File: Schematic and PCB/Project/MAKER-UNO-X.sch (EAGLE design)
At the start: 101 parts, among them CN1 USB-5PIN_(MICRO-B-RA), Q1 60V 600mA, Q10 50V 220mA, Q11 50V 220mA, Q12 50V 220mA, Q13 50V 220mA, Q14 50V 220mA, Q2 50V 220mA, Q3 50V 220mA, Q4 50V 220mA, Q5 50V 220mA, Q6 50V 220mA, Q7 50V 220mA, Q8 50V 220mA, Q9 50V 220mA, U2 CH340G_(SOIC-16N), U3 555_(SOIC-08N), U4 3.3V 500mA, Y1 16MHz

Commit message: Updated resistor value.
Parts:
- R11: value 10R -> 5R1; device Others:RESISTOR_10R_(2012) -> Others:RESISTOR_5R1_(2012)
- R4: value 1M -> 100K; device Others:RESISTOR_1M_(1608) -> Others:RESISTOR_100K_(1608)
- R5: value 22K -> 10K; device Others:RESISTOR_22K_(1608) -> Others:RESISTOR_10K_(1608)
- R9: value 1K -> 330R; device Others:RESISTOR_1K_(1608) -> Others:RESISTOR_330R_(1608)
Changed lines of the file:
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@@
 <grid distance="0.1" unitdist="inch" unit="inch" style="lines" multiple="1" display="no" altdistance="0.01" altunitdist="inch" altunit="inch"/>
 <layers>
-<layer number="1" name="Top" color="4" fill="1" visible="yes" active="no"/>
-<layer number="2" name="Route2" color="1" fill="3" visible="yes" active="no"/>
-<layer number="3" name="Route3" color="4" fill="3" visible="yes" active="no"/>
-<layer number="4" name="Route4" color="1" fill="4" visible="yes" active="no"/>
-<layer number="5" name="Route5" color="4" fill="4" visible="yes" active="no"/>
-<layer number="6" name="Route6" color="1" fill="8" visible="yes" active="no"/>
-<layer number="7" name="Route7" color="4" fill="8" visible="yes" active="no"/>
-<layer number="8" name="Route8" color="1" fill="2" visible="yes" active="no"/>
-<layer number="9" name="Route9" color="4" fill="2" visible="yes" active="no"/>
-<layer number="10" name="Route10" color="1" fill="7" visible="yes" active="no"/>
-<layer number="11" name="Route11" color="4" fill="7" visible="yes" active="no"/>
-<layer number="12" name="Route12" color="1" fill="5" visible="yes" active="no"/>
-<layer number="13" name="Route13" color="4" fill="5" visible="yes" active="no"/>
-<layer number="14" name="Route14" color="1" fill="6" visible="yes" active="no"/>
-<layer number="15" name="Route15" color="4" fill="6" visible="yes" active="no"/>
-<layer number="16" name="Bottom" color="1" fill="1" visible="yes" active="no"/>
-<layer number="17" name="Pads" color="2" fill="1" visible="yes" active="no"/>
-<layer number="18" name="Vias" color="2" fill="1" visible="yes" active="no"/>
-<layer number="19" name="Unrouted" color="6" fill="1" visible="yes" active="no"/>
-<layer number="20" name="Dimension" color="15" fill="1" visible="yes" active="no"/>
-<layer number="21" name="tPlace" color="7" fill="1" visible="yes" active="no"/>
-<layer number="22" name="bPlace" color="7" fill="1" visible="yes" active="no"/>
-<layer number="23" name="tOrigins" color="15" fill="1" visible="yes" active="no"/>
-<layer number="24" name="bOrigins" color="15" fill="1" visible="yes" active="no"/>
-<layer number="25" name="tNames" color="3" fill="1" visible="yes" active="no"/>
-<layer number="26" name="bNames" color="3" fill="1" visible="yes" active="no"/>
-<layer number="27" name="tValues" color="5" fill="1" visible="yes" active="no"/>
-<layer number="28" name="bValues" color="5" fill="1" visible="yes" active="no"/>
+<layer number="1" name="Top" color="4" fill="1" visible="no" active="no"/>
+<layer number="2" name="Route2" color="1" fill="3" visible="no" active="no"/>
+<layer number="3" name="Route3" color="4" fill="3" visible="no" active="no"/>
+<layer number="4" name="Route4" color="1" fill="4" visible="no" active="no"/>
+<layer number="5" name="Route5" color="4" fill="4" visible="no" active="no"/>
+<layer number="6" name="Route6" color="1" fill="8" visible="no" active="no"/>
+<layer number="7" name="Route7" color="4" fill="8" visible="no" active="no"/>
+<layer number="8" name="Route8" color="1" fill="2" visible="no" active="no"/>
+<layer number="9" name="Route9" color="4" fill="2" visible="no" active="no"/>
+<layer number="10" name="Route10" color="1" fill="7" visible="no" active="no"/>
+<layer number="11" name="Route11" color="4" fill="7" visible="no" active="no"/>
+<layer number="12" name="Route12" color="1" fill="5" visible="no" active="no"/>
+<layer number="13" name="Route13" color="4" fill="5" visible="no" active="no"/>
+<layer number="14" name="Route14" color="1" fill="6" visible="no" active="no"/>
+<layer number="15" name="Route15" color="4" fill="6" visible="no" active="no"/>
+<layer number="16" name="Bottom" color="1" fill="1" visible="no" active="no"/>
+<layer number="17" name="Pads" color="2" fill="1" visible="no" active="no"/>
+<layer number="18" name="Vias" color="2" fill="1" visible="no" active="no"/>
+<layer number="19" name="Unrouted" color="6" fill="1" visible="no" active="no"/>
+<layer number="20" name="Dimension" color="15" fill="1" visible="no" active="no"/>
+<layer number="21" name="tPlace" color="7" fill="1" visible="no" active="no"/>
+<layer number="22" name="bPlace" color="7" fill="1" visible="no" active="no"/>
+<layer number="23" name="tOrigins" color="15" fill="1" visible="no" active="no"/>
+<layer number="24" name="bOrigins" color="15" fill="1" visible="no" active="no"/>
+<layer number="25" name="tNames" color="3" fill="1" visible="no" active="no"/>
+<layer number="26" name="bNames" color="3" fill="1" visible="no" active="no"/>
+<layer number="27" name="tValues" color="5" fill="1" visible="no" active="no"/>
+<layer number="28" name="bValues" color="5" fill="1" visible="no" active="no"/>
 <layer number="29" name="tStop" color="7" fill="3" visible="no" active="no"/>
 <layer number="30" name="bStop" color="7" fill="6" visible="no" active="no"/>
@@
 <layer number="35" name="tGlue" color="7" fill="4" visible="no" active="no"/>
 <layer number="36" name="bGlue" color="7" fill="5" visible="no" active="no"/>
-<layer number="37" name="tTest" color="7" fill="1" visible="yes" active="no"/>
-<layer number="38" name="bTest" color="7" fill="1" visible="yes" active="no"/>
+<layer number="37" name="tTest" color="7" fill="1" visible="no" active="no"/>
+<layer number="38" name="bTest" color="7" fill="1" visible="no" active="no"/>
 <layer number="39" name="tKeepout" color="4" fill="11" visible="no" active="no"/>
 <layer number="40" name="bKeepout" color="1" fill="11" visible="no" active="no"/>
@@
 <layer number="44" name="Drills" color="7" fill="1" visible="no" active="no"/>
 <layer number="45" name="Holes" color="7" fill="1" visible="no" active="no"/>
-<layer number="46" name="Milling" color="3" fill="1" visible="yes" active="no"/>
-<layer number="47" name="Measures" color="7" fill="1" visible="yes" active="no"/>
-<layer number="48" name="Document" color="7" fill="1" visible="yes" active="no"/>
-<layer number="49" name="Reference" color="7" fill="1" visible="yes" active="no"/>
-<layer number="50" name="dxf" color="7" fill="1" visible="yes" active="no"/>
-<layer number="51" name="tDocu" color="6" fill="1" visible="yes" active="no"/>
-<layer number="52" name="bDocu" color="6" fill="1" visible="yes" active="no"/>
-<layer number="53" name="tGND_GNDA" color="7" fill="9" visible="yes" active="no"/>
-<layer number="54" name="bGND_GNDA" color="1" fill="9" visible="yes" active="no"/>
-<layer number="56" name="wert" color="7" fill="1" visible="yes" active="no"/>
-<layer number="57" name="tCAD" color="7" fill="1" visible="yes" active="no"/>
-<layer number="59" name="tCarbon" color="7" fill="1" visible="yes" active="no"/>
-<layer number="60" name="bCarbon" color="7" fill="1" visible="yes" active="no"/>
+<layer number="46" name="Milling" color="3" fill="1" visible="no" active="no"/>
+<layer number="47" name="Measures" color="7" fill="1" visible="no" active="no"/>
+<layer number="48" name="Document" color="7" fill="1" visible="no" active="no"/>
+<layer number="49" name="Reference" color="7" fill="1" visible="no" active="no"/>
+<layer number="50" name="dxf" color="7" fill="1" visible="no" active="no"/>
+<layer number="51" name="tDocu" color="6" fill="1" visible="no" active="no"/>
+<layer number="52" name="bDocu" color="6" fill="1" visible="no" active="no"/>
+<layer number="53" name="tGND_GNDA" color="7" fill="9" visible="no" active="no"/>
+<layer number="54" name="bGND_GNDA" color="1" fill="9" visible="no" active="no"/>
+<layer number="56" name="wert" color="7" fill="1" visible="no" active="no"/>
+<layer number="57" name="tCAD" color="7" fill="1" visible="no" active="no"/>
+<layer number="59" name="tCarbon" color="7" fill="1" visible="no" active="no"/>
+<layer number="60" name="bCarbon" color="7" fill="1" visible="no" active="no"/>
 <layer number="90" name="Modules" color="5" fill="1" visible="yes" active="yes"/>
 <layer number="91" name="Nets" color="2" fill="1" visible="yes" active="yes"/>
@@
 <part name="GND34" library="Supply" deviceset="GND" device=""/>
 <part name="C12" library="Others" deviceset="CAP-C" device="_(1608)" technology="_0.1UF" value="0.1uF"/>
-<part name="R4" library="Others" deviceset="RESISTOR" device="_(1608)" technology="_1M" value="1M"/>
+<part name="R4" library="Others" deviceset="RESISTOR" device="_(1608)" technology="_100K" value="100K"/>
 <part name="GND35" library="Supply" deviceset="GND" device=""/>
 <part name="C11" library="Others" deviceset="CAP-C" device="_(1608)" technology="_10NF" value="10nF"/>
@@
 <part name="C9" library="Others" deviceset="CAP-C" device="_(2012)" technology="_10UF" value="10uF"/>
 <part name="GND37" library="Supply" deviceset="GND" device=""/>
-<part name="R9" library="Others" deviceset="RESISTOR" device="_(1608)" technology="_1K" value="1K"/>
-<part name="R5" library="Others" deviceset="RESISTOR" device="_(1608)" technology="_22K" value="22K"/>
+<part name="R9" library="Others" deviceset="RESISTOR" device="_(1608)" technology="_330R" value="330R"/>
+<part name="R5" library="Others" deviceset="RESISTOR" device="_(1608)" technology="_10K" value="10K"/>
 <part name="Q1" library="IC &amp; Transistor" deviceset="TRANSISTOR-PNP" device="_(SOT-23-BEC)" technology="_MMBT2907" value="60V 600mA"/>
-<part name="R11" library="Others" deviceset="RESISTOR" device="_(2012)" technology="_10R" value="10R"/>
+<part name="R11" library="Others" deviceset="RESISTOR" device="_(2012)" technology="_5R1" value="5R1"/>
 <part name="R12" library="Others" deviceset="RESISTOR" device="_(2012)" technology="_10R" value="10R"/>
 <part name="GND38" library="Supply" deviceset="GND" device=""/>

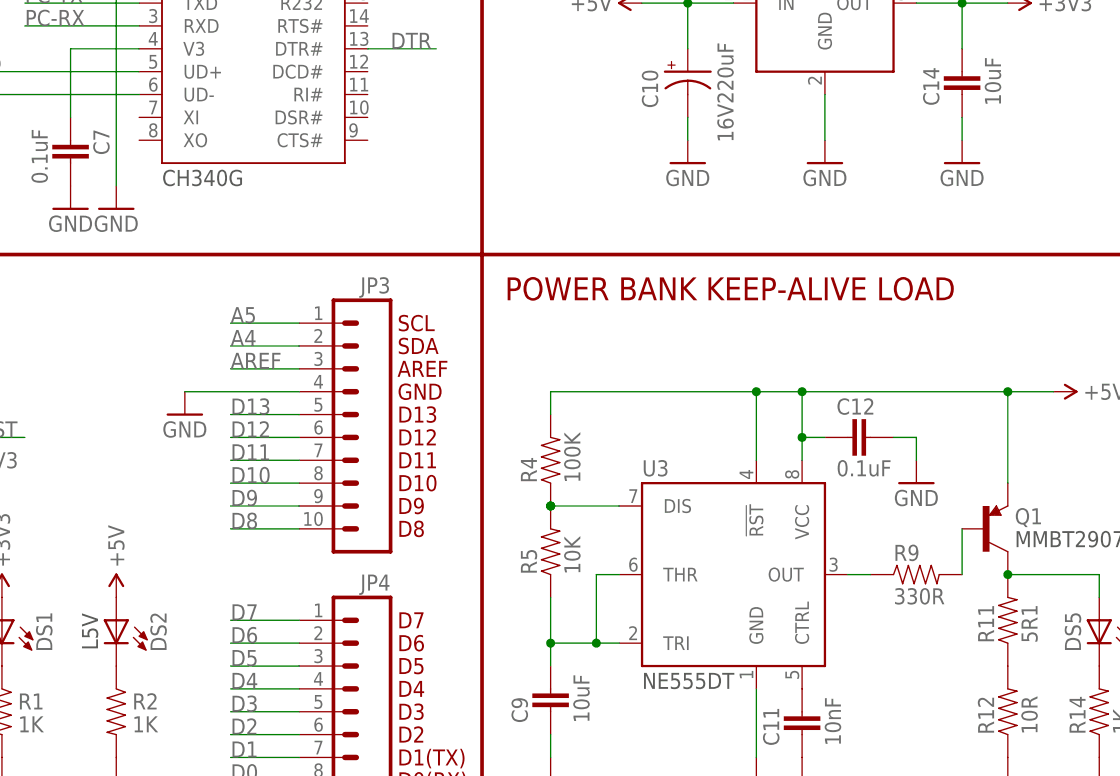
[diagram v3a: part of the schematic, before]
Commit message: Updated resistor value.
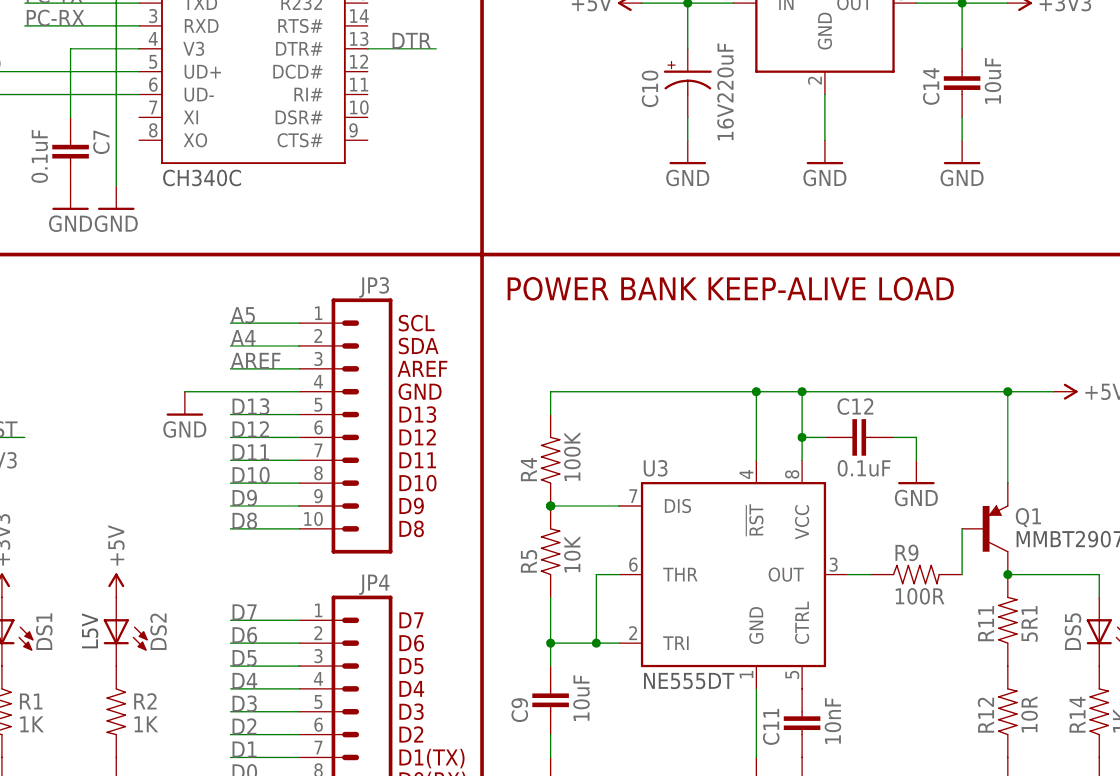
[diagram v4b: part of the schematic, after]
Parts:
- R9: value 330R -> 100R; device Others:RESISTOR_330R_(1608) -> Others:RESISTOR_100R_(1608)
- U2: value CH340G_(SOIC-16N) -> CH340G_CH340C_(SOIC-16N); device IC & Transistor:CH340G_(SOIC-16N) -> IC & Transistor:CH340G_CH340C_(SOIC-16N)
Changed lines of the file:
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@@
 <grid distance="0.1" unitdist="inch" unit="inch" style="lines" multiple="1" display="no" altdistance="0.01" altunitdist="inch" altunit="inch"/>
 <layers>
-<layer number="1" name="Top" color="4" fill="1" visible="no" active="no"/>
-<layer number="2" name="Route2" color="1" fill="3" visible="no" active="no"/>
-<layer number="3" name="Route3" color="4" fill="3" visible="no" active="no"/>
-<layer number="4" name="Route4" color="1" fill="4" visible="no" active="no"/>
-<layer number="5" name="Route5" color="4" fill="4" visible="no" active="no"/>
-<layer number="6" name="Route6" color="1" fill="8" visible="no" active="no"/>
-<layer number="7" name="Route7" color="4" fill="8" visible="no" active="no"/>
-<layer number="8" name="Route8" color="1" fill="2" visible="no" active="no"/>
-<layer number="9" name="Route9" color="4" fill="2" visible="no" active="no"/>
-<layer number="10" name="Route10" color="1" fill="7" visible="no" active="no"/>
-<layer number="11" name="Route11" color="4" fill="7" visible="no" active="no"/>
-<layer number="12" name="Route12" color="1" fill="5" visible="no" active="no"/>
-<layer number="13" name="Route13" color="4" fill="5" visible="no" active="no"/>
-<layer number="14" name="Route14" color="1" fill="6" visible="no" active="no"/>
-<layer number="15" name="Route15" color="4" fill="6" visible="no" active="no"/>
-<layer number="16" name="Bottom" color="1" fill="1" visible="no" active="no"/>
-<layer number="17" name="Pads" color="2" fill="1" visible="no" active="no"/>
-<layer number="18" name="Vias" color="2" fill="1" visible="no" active="no"/>
-<layer number="19" name="Unrouted" color="6" fill="1" visible="no" active="no"/>
-<layer number="20" name="Dimension" color="15" fill="1" visible="no" active="no"/>
-<layer number="21" name="tPlace" color="7" fill="1" visible="no" active="no"/>
-<layer number="22" name="bPlace" color="7" fill="1" visible="no" active="no"/>
-<layer number="23" name="tOrigins" color="15" fill="1" visible="no" active="no"/>
-<layer number="24" name="bOrigins" color="15" fill="1" visible="no" active="no"/>
-<layer number="25" name="tNames" color="3" fill="1" visible="no" active="no"/>
-<layer number="26" name="bNames" color="3" fill="1" visible="no" active="no"/>
-<layer number="27" name="tValues" color="5" fill="1" visible="no" active="no"/>
-<layer number="28" name="bValues" color="5" fill="1" visible="no" active="no"/>
+<layer number="1" name="Top" color="4" fill="1" visible="yes" active="no"/>
+<layer number="2" name="Route2" color="1" fill="3" visible="yes" active="no"/>
+<layer number="3" name="Route3" color="4" fill="3" visible="yes" active="no"/>
+<layer number="4" name="Route4" color="1" fill="4" visible="yes" active="no"/>
+<layer number="5" name="Route5" color="4" fill="4" visible="yes" active="no"/>
+<layer number="6" name="Route6" color="1" fill="8" visible="yes" active="no"/>
+<layer number="7" name="Route7" color="4" fill="8" visible="yes" active="no"/>
+<layer number="8" name="Route8" color="1" fill="2" visible="yes" active="no"/>
+<layer number="9" name="Route9" color="4" fill="2" visible="yes" active="no"/>
+<layer number="10" name="Route10" color="1" fill="7" visible="yes" active="no"/>
+<layer number="11" name="Route11" color="4" fill="7" visible="yes" active="no"/>
+<layer number="12" name="Route12" color="1" fill="5" visible="yes" active="no"/>
+<layer number="13" name="Route13" color="4" fill="5" visible="yes" active="no"/>
+<layer number="14" name="Route14" color="1" fill="6" visible="yes" active="no"/>
+<layer number="15" name="Route15" color="4" fill="6" visible="yes" active="no"/>
+<layer number="16" name="Bottom" color="1" fill="1" visible="yes" active="no"/>
+<layer number="17" name="Pads" color="2" fill="1" visible="yes" active="no"/>
+<layer number="18" name="Vias" color="2" fill="1" visible="yes" active="no"/>
+<layer number="19" name="Unrouted" color="6" fill="1" visible="yes" active="no"/>
+<layer number="20" name="Dimension" color="15" fill="1" visible="yes" active="no"/>
+<layer number="21" name="tPlace" color="7" fill="1" visible="yes" active="no"/>
+<layer number="22" name="bPlace" color="7" fill="1" visible="yes" active="no"/>
+<layer number="23" name="tOrigins" color="15" fill="1" visible="yes" active="no"/>
+<layer number="24" name="bOrigins" color="15" fill="1" visible="yes" active="no"/>
+<layer number="25" name="tNames" color="3" fill="1" visible="yes" active="no"/>
+<layer number="26" name="bNames" color="3" fill="1" visible="yes" active="no"/>
+<layer number="27" name="tValues" color="5" fill="1" visible="yes" active="no"/>
+<layer number="28" name="bValues" color="5" fill="1" visible="yes" active="no"/>
 <layer number="29" name="tStop" color="7" fill="3" visible="no" active="no"/>
 <layer number="30" name="bStop" color="7" fill="6" visible="no" active="no"/>
@@
 <layer number="35" name="tGlue" color="7" fill="4" visible="no" active="no"/>
 <layer number="36" name="bGlue" color="7" fill="5" visible="no" active="no"/>
-<layer number="37" name="tTest" color="7" fill="1" visible="no" active="no"/>
-<layer number="38" name="bTest" color="7" fill="1" visible="no" active="no"/>
+<layer number="37" name="tTest" color="7" fill="1" visible="yes" active="no"/>
+<layer number="38" name="bTest" color="7" fill="1" visible="yes" active="no"/>
 <layer number="39" name="tKeepout" color="4" fill="11" visible="no" active="no"/>
 <layer number="40" name="bKeepout" color="1" fill="11" visible="no" active="no"/>
@@
 <layer number="44" name="Drills" color="7" fill="1" visible="no" active="no"/>
 <layer number="45" name="Holes" color="7" fill="1" visible="no" active="no"/>
-<layer number="46" name="Milling" color="3" fill="1" visible="no" active="no"/>
-<layer number="47" name="Measures" color="7" fill="1" visible="no" active="no"/>
-<layer number="48" name="Document" color="7" fill="1" visible="no" active="no"/>
-<layer number="49" name="Reference" color="7" fill="1" visible="no" active="no"/>
-<layer number="50" name="dxf" color="7" fill="1" visible="no" active="no"/>
-<layer number="51" name="tDocu" color="6" fill="1" visible="no" active="no"/>
-<layer number="52" name="bDocu" color="6" fill="1" visible="no" active="no"/>
-<layer number="53" name="tGND_GNDA" color="7" fill="9" visible="no" active="no"/>
-<layer number="54" name="bGND_GNDA" color="1" fill="9" visible="no" active="no"/>
-<layer number="56" name="wert" color="7" fill="1" visible="no" active="no"/>
-<layer number="57" name="tCAD" color="7" fill="1" visible="no" active="no"/>
-<layer number="59" name="tCarbon" color="7" fill="1" visible="no" active="no"/>
-<layer number="60" name="bCarbon" color="7" fill="1" visible="no" active="no"/>
+<layer number="46" name="Milling" color="3" fill="1" visible="yes" active="no"/>
+<layer number="47" name="Measures" color="7" fill="1" visible="yes" active="no"/>
+<layer number="48" name="Document" color="7" fill="1" visible="yes" active="no"/>
+<layer number="49" name="Reference" color="7" fill="1" visible="yes" active="no"/>
+<layer number="50" name="dxf" color="7" fill="1" visible="yes" active="no"/>
+<layer number="51" name="tDocu" color="6" fill="1" visible="yes" active="no"/>
+<layer number="52" name="bDocu" color="6" fill="1" visible="yes" active="no"/>
+<layer number="53" name="tGND_GNDA" color="7" fill="9" visible="yes" active="no"/>
+<layer number="54" name="bGND_GNDA" color="1" fill="9" visible="yes" active="no"/>
+<layer number="56" name="wert" color="7" fill="1" visible="yes" active="no"/>
+<layer number="57" name="tCAD" color="7" fill="1" visible="yes" active="no"/>
+<layer number="59" name="tCarbon" color="7" fill="1" visible="yes" active="no"/>
+<layer number="60" name="bCarbon" color="7" fill="1" visible="yes" active="no"/>
 <layer number="90" name="Modules" color="5" fill="1" visible="yes" active="yes"/>
 <layer number="91" name="Nets" color="2" fill="1" visible="yes" active="yes"/>
@@
 <part name="JP4" library="Header and Connector" deviceset="HEADER-1X08" device="_(SMD-FEMALE-TYPE1)" value="8 Ways"/>
 <part name="JP3" library="Header and Connector" deviceset="HEADER-1X10" device="_(SMD-FEMALE-TYPE1)" value="10 Ways"/>
-<part name="U2" library="IC &amp; Transistor" deviceset="CH340G" device="_(SOIC-16N)"/>
+<part name="U2" library="IC &amp; Transistor" deviceset="CH340G" device="_(SOIC-16N)" technology="_CH340C" value=""/>
 <part name="DS17" library="Others" deviceset="LED" device="_(1608)" technology="_BLUE" value="Blue">
 <attribute name="LABEL" value="L13"/>
@@
 <part name="C9" library="Others" deviceset="CAP-C" device="_(2012)" technology="_10UF" value="10uF"/>
 <part name="GND37" library="Supply" deviceset="GND" device=""/>
-<part name="R9" library="Others" deviceset="RESISTOR" device="_(1608)" technology="_330R" value="330R"/>
+<part name="R9" library="Others" deviceset="RESISTOR" device="_(1608)" technology="_100R" value="100R"/>
 <part name="R5" library="Others" deviceset="RESISTOR" device="_(1608)" technology="_10K" value="10K"/>
 <part name="Q1" library="IC &amp; Transistor" deviceset="TRANSISTOR-PNP" device="_(SOT-23-BEC)" technology="_MMBT2907" value="60V 600mA"/>
